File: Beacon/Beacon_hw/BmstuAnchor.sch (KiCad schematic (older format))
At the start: 46 parts, among them SW1 SW_PUSH, U1 MCP1700T-3002E/TT

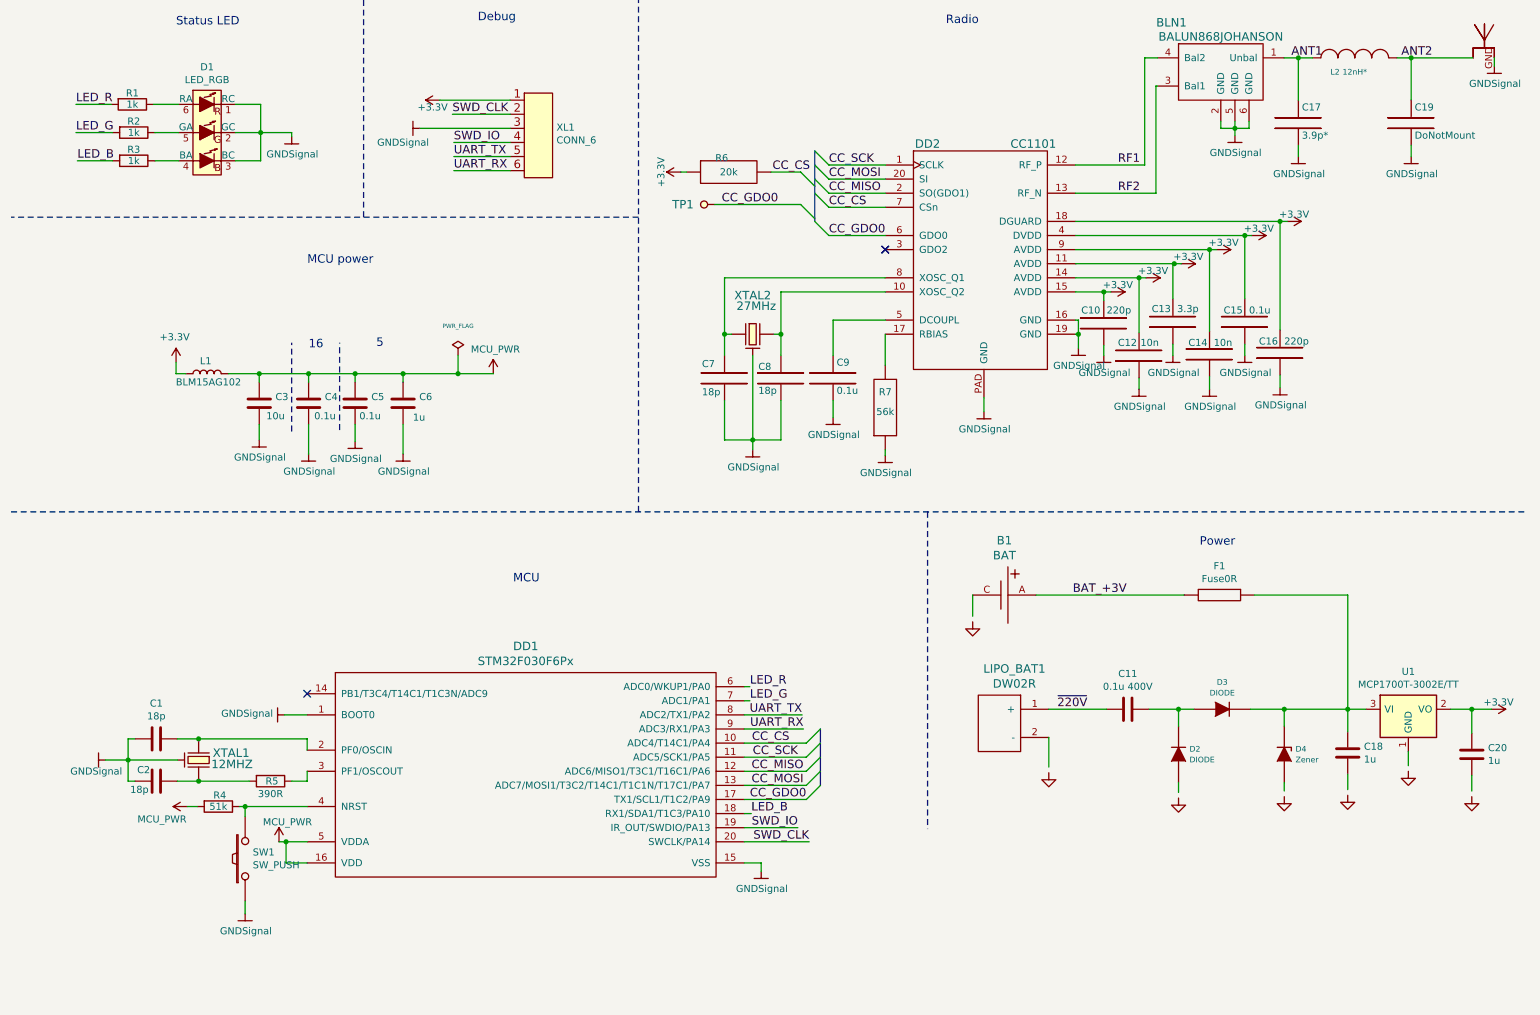
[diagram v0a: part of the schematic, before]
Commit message: +beacon pcb
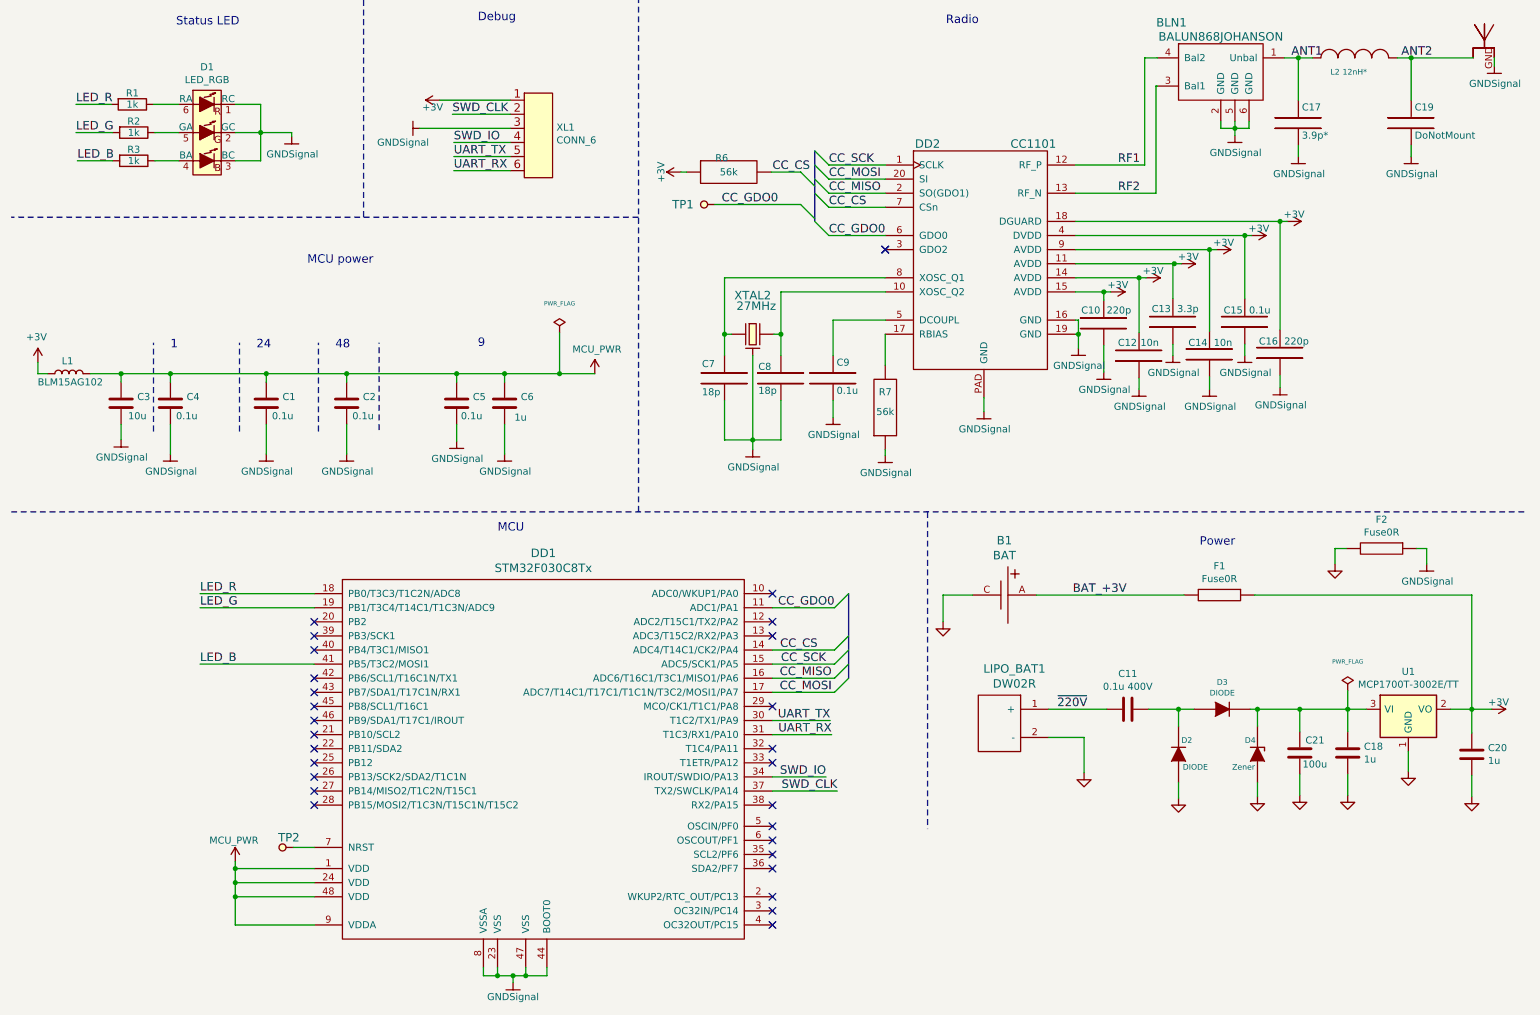
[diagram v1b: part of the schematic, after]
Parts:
- removed DD1: STM32F030F6Px, SO_DIL_TSSOP:TSSOP20, symbol STM32F030F6Px
- removed R4: 51k, Resistors:RES_0603, symbol R
- removed R5: 390R, Resistors:RES_0603, symbol R
- removed SW1: SW_PUSH, BtnsSwitches:BTN_6x6_4x4, symbol SW_PUSH
- removed XTAL1: 12MHZ, Quartz:0503x4-4, symbol CRYSTAL_H
- added C21: 100u, Capacitors:CAP_1210, symbol C
- added DD1: STM32F030C8Tx, LQFP_TQFP:LQFP48, symbol STM32F030C8Tx
- added F2: Fuse0R, Resistors:RES_0603_FUSE, symbol Fuse0R
- added TP2: TESTPOINT, PCB:TESTPOINT_1MM, symbol TESTPOINT
- C1, C2: value 18p -> 0.1u
- C11: footprint (none) -> Capacitors:CAP_1812
- D2, D3: footprint (none) -> Diodes:SMA_DO214AC
- D4: footprint (none) -> SOT:SOT23-3
- LIPO_BAT1: footprint (none) -> Connectors:PLS-2-wide
- R6: value 20k -> 56k
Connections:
- net labels added: +3V
- net labels removed: +3.3V
- wire segments 140 -> 145
- no-connect marks 3 -> 29
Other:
- note added: "1"
- note added: "24"
- note added: "48"
- note added: "9"
- note removed: "16"
- note removed: "5"
- moved on the sheet: C3, C4, C5, C6, D4, L1

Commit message: *pcb upd, C before antenna added
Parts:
- added C?: 100pF, Capacitors:CAP_0402, symbol C-RESCUE-Badge
- C10, C16: value 220p -> 0.1u
- C12, C14: value 10n -> 0.1u
- C13: value 3.3p -> 0.1u
- D4: symbol Zener -> Zener-RESCUE-BmstuAnchor
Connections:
- net +3V: no longer XL1.1
- net ANT2: now also C?.2; no longer D5.~
- net GND: now also D4.1; no longer D4.A
- net MCU_PWR: now also XL1.1
- net at C18.1, C21.1, D3.C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: now also D4.3; no longer D4.C
- new net: C?.1, D5.~
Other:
- moved on the sheet: BLN1, C10, C12, C13, C14, C15, C16, C17, C19, C7, C8, C9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

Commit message: +axp library *beaco pcb upd
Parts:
- removed F1: Fuse0R, Resistors:RES_0603_FUSE, symbol Fuse0R
- gave numbers to parts that had none: 1
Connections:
- net BAT_+3V is gone; now on net +3V: B1.A
- net GND: no longer B1.C
- net GNDS: now also B1.C
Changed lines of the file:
@@
 $EndComp
 $Comp
-L +3V #PWR28
+L +3V #PWR27
 U 1 1 59933ABE
 P 8710 2450
-F 0 "#PWR28" H 8710 2300 50  0001 C CNN
+F 0 "#PWR27" H 8710 2300 50  0001 C CNN
 F 1 "+3V" V 8660 2500 50  0000 C CNN
 F 2 "" H 8710 2450 50  0000 C CNN
@@
 $EndComp
 $Comp
-L GNDSignal #PWR42
+L GNDSignal #PWR41
 U 1 1 59933B3C
 P 10340 1690
-F 0 "#PWR42" H 10390 1740 50  0001 C CNN
+F 0 "#PWR41" H 10390 1740 50  0001 C CNN
 F 1 "GNDSignal" H 10345 1567 50  0000 C CNN
 F 2 "" H -12490 -1330 50  0000 C CNN
@@
 $EndComp
 $Comp
-L GND #PWR27
+L GND #PWR28
 U 1 1 59A07A5C
 P 8750 6320
-F 0 "#PWR27" H 8800 6370 30  0001 C CNN
+F 0 "#PWR28" H 8800 6370 30  0001 C CNN
 F 1 "GND" H 2520 -50 30  0001 C CNN
 F 2 "" H 2520 30  60  0000 C CNN
@@
 $EndComp
 $Comp
-L GND #PWR41
+L GND #PWR42
 U 1 1 59A07C48
 P 10380 6130
-F 0 "#PWR41" H 10430 6180 30  0001 C CNN
+F 0 "#PWR42" H 10430 6180 30  0001 C CNN
 F 1 "GND" H 4150 -240 30  0001 C CNN
 F 2 "" H 4150 -160 60  0000 C CNN
 F 3 "" H 4150 -160 60  0000 C CNN
 	1    10380 6130
-	1    0    0    -1
-$EndComp
-$Comp
-L GND #PWR18
-U 1 1 59A08526
-P 7080 5070
-F 0 "#PWR18" H 7130 5120 30  0001 C CNN
-F 1 "GND" H 850 -1300 30  0001 C CNN
-F 2 "" H 850 -1220 60  0000 C CNN
-F 3 "" H 850 -1220 60  0000 C CNN
-	1    7080 5070
 	1    0    0    -1
 $EndComp
@@
 $EndComp
 $Comp
-L Fuse0R F1
-U 1 1 59A01B33
-P 9040 4880
-F 0 "F1" V 8834 4880 50  0000 C CNN
-F 1 "Fuse0R" V 8925 4880 50  0000 C CNN
-F 2 "Resistors:RES_0603_FUSE" V -180 -100 60  0001 C CNN
-F 3 "" V -80 0   60  0001 C CNN
-F 4 "1" V 20  100 60  0001 C CNN "SolderPoints"
-F 5 "0" V 120 200 60  0001 C CNN "Price"
-	1    9040 4880
-	0    1    1    0
-$EndComp
-$Comp
 L STM32F030C8Tx DD1
 U 1 1 59A7451E
@@
 Connection ~ 10830 5690
 Wire Wire Line
-	9290 4880 10830 4880
-Wire Wire Line
-	8790 4880 7740 4880
+	7740 4880 10830 4880
 Wire Wire Line
 	2620 4870 1810 4870
@@
 	10510 4550 10510 4660
 $Comp
-L MCU_PWR #PWR?
+L MCU_PWR #PWR9
 U 1 1 5A003795
 P 3510 1370
-F 0 "#PWR?" H 1140 -1770 50  0001 C CNN
+F 0 "#PWR9" H 1140 -1770 50  0001 C CNN
 F 1 "MCU_PWR" V 3580 1430 50  0000 C CNN
 F 2 "" H 1140 -1620 50  0000 C CNN
@@
 $EndComp
 $Comp
-L C-RESCUE-Badge C?
+L C-RESCUE-Badge C22
 U 1 1 5A006874
 P 10610 990
-F 0 "C?" V 10390 940 50  0000 L CNN
+F 0 "C22" V 10390 940 50  0000 L CNN
 F 1 "100pF" V 10810 870 50  0000 L CNN
 F 2 "Capacitors:CAP_0402" H 10648 840 50  0001 C CNN
@@
 Wire Wire Line
 	10760 990  10850 990
+$Comp
+L GNDSignal #PWR?
+U 1 1 5A081B45
+P 7080 5070
+F 0 "#PWR?" H 7130 5120 50  0001 C CNN
+F 1 "GNDSignal" H 7085 4947 50  0000 C CNN
+F 2 "" H -15750 2050 50  0000 C CNN
+F 3 "" H -15750 2050 50  0000 C CNN
+	1    7080 5070
+	1    0    0    -1
+$EndComp
 $EndSCHEMATC

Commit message: display lib upd
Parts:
- removed C1, C2, C4, C5: 0.1u, Capacitors:CAP_0603, symbol C
- removed C11: 0.1u 400V, Capacitors:CAP_1812, symbol C
- removed C18, C20, C6: 1u, Capacitors:CAP_0603, symbol C
- removed C21: 100u, Capacitors:CAP_1210, symbol C
- removed C3: 10u, Capacitors:CAP_0603, symbol C
- removed D2, D3: DIODE, Diodes:SMA_DO214AC, symbol DIODE
- removed D4: Zener, SOT:SOT23-3, symbol Zener-RESCUE-BmstuAnchor
- removed F2: Fuse0R, Resistors:RES_0603_FUSE, symbol Fuse0R
- removed L1: BLM15AG102, Inductors:IND_0402, symbol L
- removed R1, R2, R3: 1k, Resistors:RES_0603, symbol R
- added C1: 10u, Capacitors:CAP_0603, symbol C-RESCUE-Badge
- added C11: 0.1u 400V, Capacitors:CAP_0603, symbol C-RESCUE-Badge
- added C18: 100u, Capacitors:CAP_0603, symbol C-RESCUE-Badge
- added C2, C3, C4, C5: 0.1u, Capacitors:CAP_0603, symbol C-RESCUE-Badge
- added C20, C21, C6: 1u, Capacitors:CAP_0603, symbol C-RESCUE-Badge
- added D2, D3: SM4004, symbol D
- added L1: BLM15AG102, Inductors:IND_0402, symbol L-RESCUE-Badge
- added R1, R2, R3: 1k, Resistors:RES_0603, symbol R-RESCUE-Badge
- added R4: 0R, Resistors:RES_0603, symbol R-RESCUE-Badge
- added VD1: BZX64C5V1LT1G, symbol VD
- U1: value MCP1700T-3002E/TT -> MCP1700T-3302E/TT
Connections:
- net +3V: now also C21.1, L1.2
- net GND: now also C18.2, C20.2, C21.2, D2.2 (A), R4.2, VD1.2 (A)
- net GNDS: now also C1.2, C2.2, C3.2, C4.2, C5.2, C6.2, R4.1
- net LED_B: now also R3.2
- net LED_G: now also R2.2
- net LED_R: now also R1.2
- net MCU_PWR: now also C1.1, C2.1, C3.1, C4.1, C5.1, C6.1, L1.1
- net ~220V: now also C11.2
- net at U1.3 (VI): now also C18.1, C20.1, D3.1 (K), VD1.1 (K)
- net at D1.4 (BA): now also R3.1
- net at D1.5 (GA): now also R2.1
- net at D1.6 (RA): now also R1.1
- new net: C11.1, D2.1 (K), D3.2 (A)
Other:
- note added: "Блок питания"
- note added: "Микроконтроллер"
- note added: "Радиочастотный тракт"
- note added: "Разъем программирования и отладки\nмикроконтроллера"
- note added: "Система индикации"
- note added: "Соединение аналоговой земли \nс цифровой землей"
- note added: "Фильтр питания микроконтроллера"
- note removed: "Debug"
- note removed: "MCU"
- note removed: "MCU power"
- note removed: "Power"
- note removed: "Radio"
- note removed: "Status LED"
- moved on the sheet: B1, BLN1, C10, C12, C13, C14, C15, C16, C17, C19, C22, C7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

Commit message: badge
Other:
- note added: "Analog to digital GND"
- note added: "Connector"
- note added: "LEDs"
- note added: "MCU unit"
- note added: "Power supply filtering"
- note added: "Power supply unit"
- note added: "RF part"
- note removed: "Блок питания"
- note removed: "Микроконтроллер"
- note removed: "Радиочастотный тракт"
- note removed: "Разъем программирования и отладки\nмикроконтроллера"
- note removed: "Система индикации"
- note removed: "Соединение аналоговой земли \nс цифровой землей"
- note removed: "Фильтр питания микроконтроллера"
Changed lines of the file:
@@
 ANT2
 Text Notes 13890 4760 0    197  ~ 39
-Радиочастотный тракт
+RF part
 NoConn ~ 13600 6310
 $Comp
@@
 LED_B
 Text Notes 15810 1950 0    197  ~ 39
-Разъем программирования и отладки\nмикроконтроллера
+Connector
 Text Notes 4460 1910 0    197  ~ 39
-Система индикации
+LEDs
 Text Notes 2900 5190 0    197  ~ 39
-Фильтр питания микроконтроллера
+Power supply filtering
 Text Notes 3950 9740 0    197  ~ 39
-Микроконтроллер
+MCU unit
 Text Notes 17740 9710 0    197  ~ 39
-Блок питания
+Power supply unit
 $Comp
 L GND #PWR45
@@
 $EndComp
 Text Notes 9840 10200 0    197  ~ 39
-Соединение аналоговой земли \nс цифровой землей
+Analog to digital GND
 Wire Notes Line
 	470  3880 22920 3880
